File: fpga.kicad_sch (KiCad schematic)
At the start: 17 parts, among them U201 ICE40HX4K, U202 W25Q16DVSS, U203 IS61WV25616FBLL-10TLI

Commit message: Schematic update
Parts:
- added C201, C202, C203, C204, C205, C206, C207, C208, C209, C210, C211, C212, C213, C214, C215: 100n, Capacitor_SMD:C_0805_2012Metric, symbol Device:C
- C216: renamed from C201; footprint (none) -> Capacitor_SMD:CP_Elec_4x5.8; Tolerance (none) -> 20%
- C217: renamed from C202; Spec1 (none) -> 16V; Spec2 (none) -> X5R; Tolerance (none) -> 20%
- C218: renamed from C203; footprint (none) -> Capacitor_SMD:CP_Elec_4x5.8; Tolerance (none) -> 20%
- C219: renamed from C204; Spec1 (none) -> 16V; Spec2 (none) -> X5R; Tolerance (none) -> 20%
- JP201: footprint (none) -> Connector_PinHeader_2.54mm:PinHeader_2x02_P2.54mm_Vertical
- JP202: footprint (none) -> Connector_PinHeader_2.54mm:PinHeader_1x02_P2.54mm_Vertical
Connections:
- net +1.2VD: now also C201.1, C202.1, C203.1, C204.1
- net +3.3VD: now also C205.1, C206.1, C207.1, C208.1, C209.1, C210.1, C211.1, C212.1, C213.1, C214.1, C215.1
- net GND: now also C201.2, C202.2, C203.2, C204.2, C205.2, C206.2, C207.2, C208.2, C209.2, C210.2, C211.2, C212.2, C213.2, C214.2, C215.2
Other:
- moved on the sheet: C216, C217, C218, C219, JP201, JP202, R201, R202, R203, R204, R205, R206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

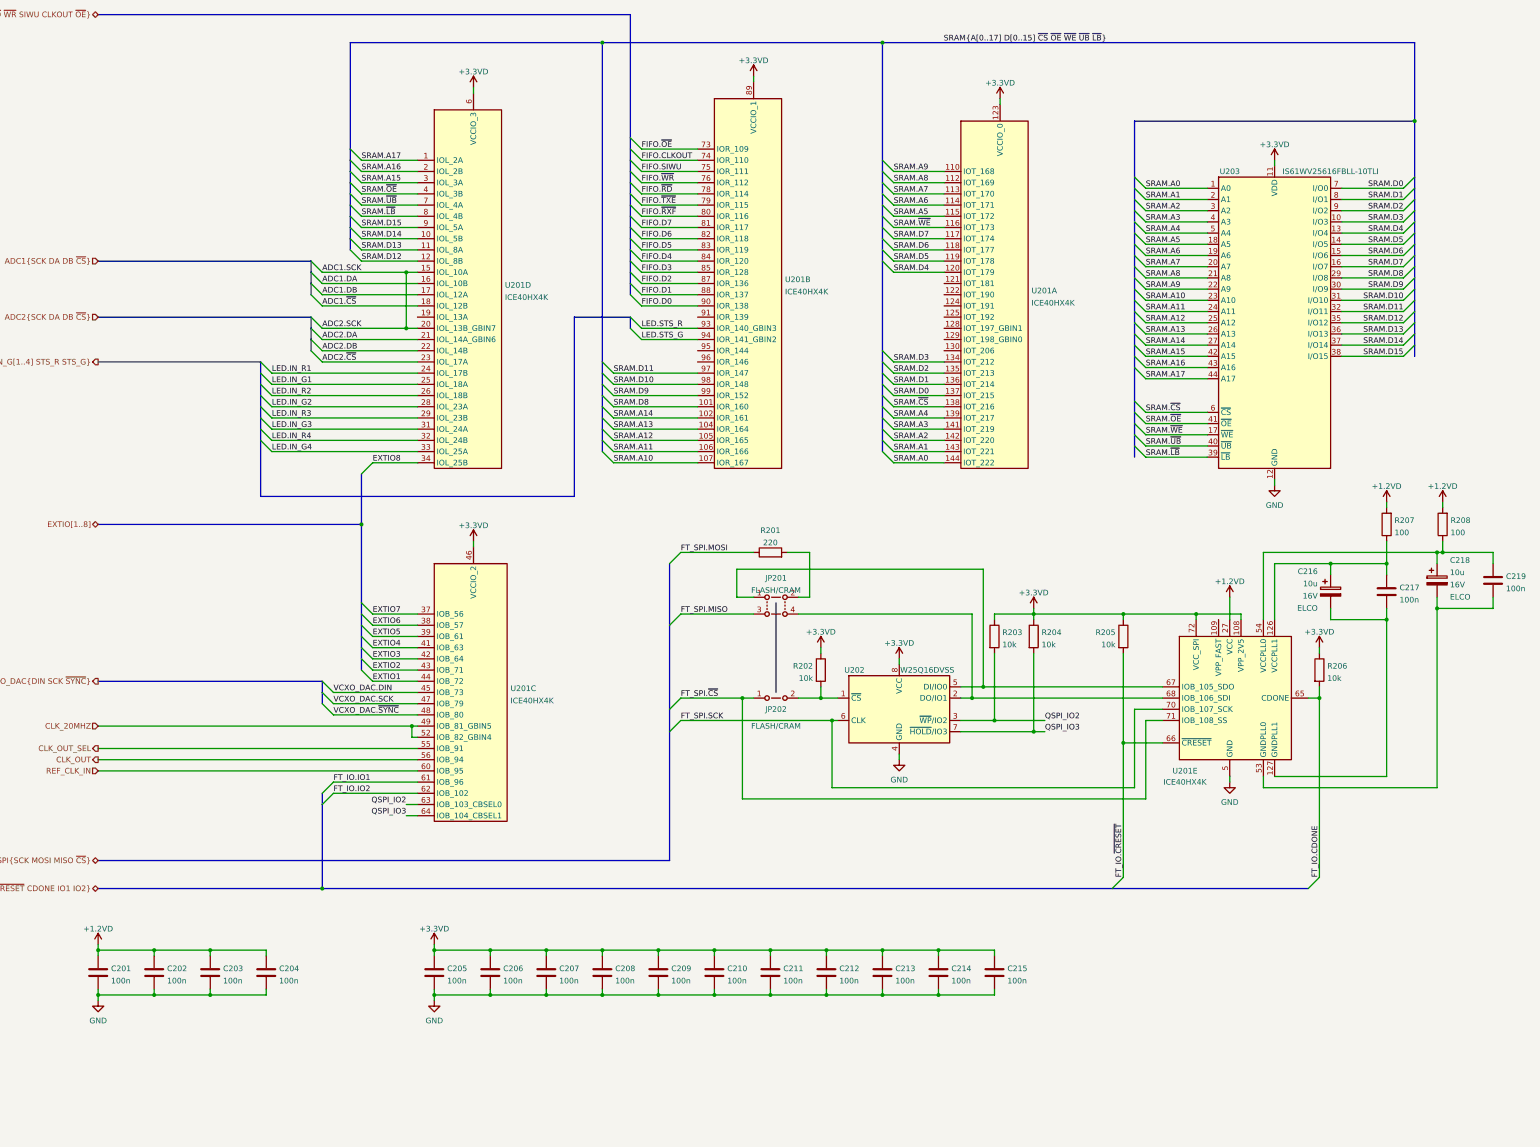
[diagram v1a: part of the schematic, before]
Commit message: Schematic: better LDO output capacitor selection, clarified BOM
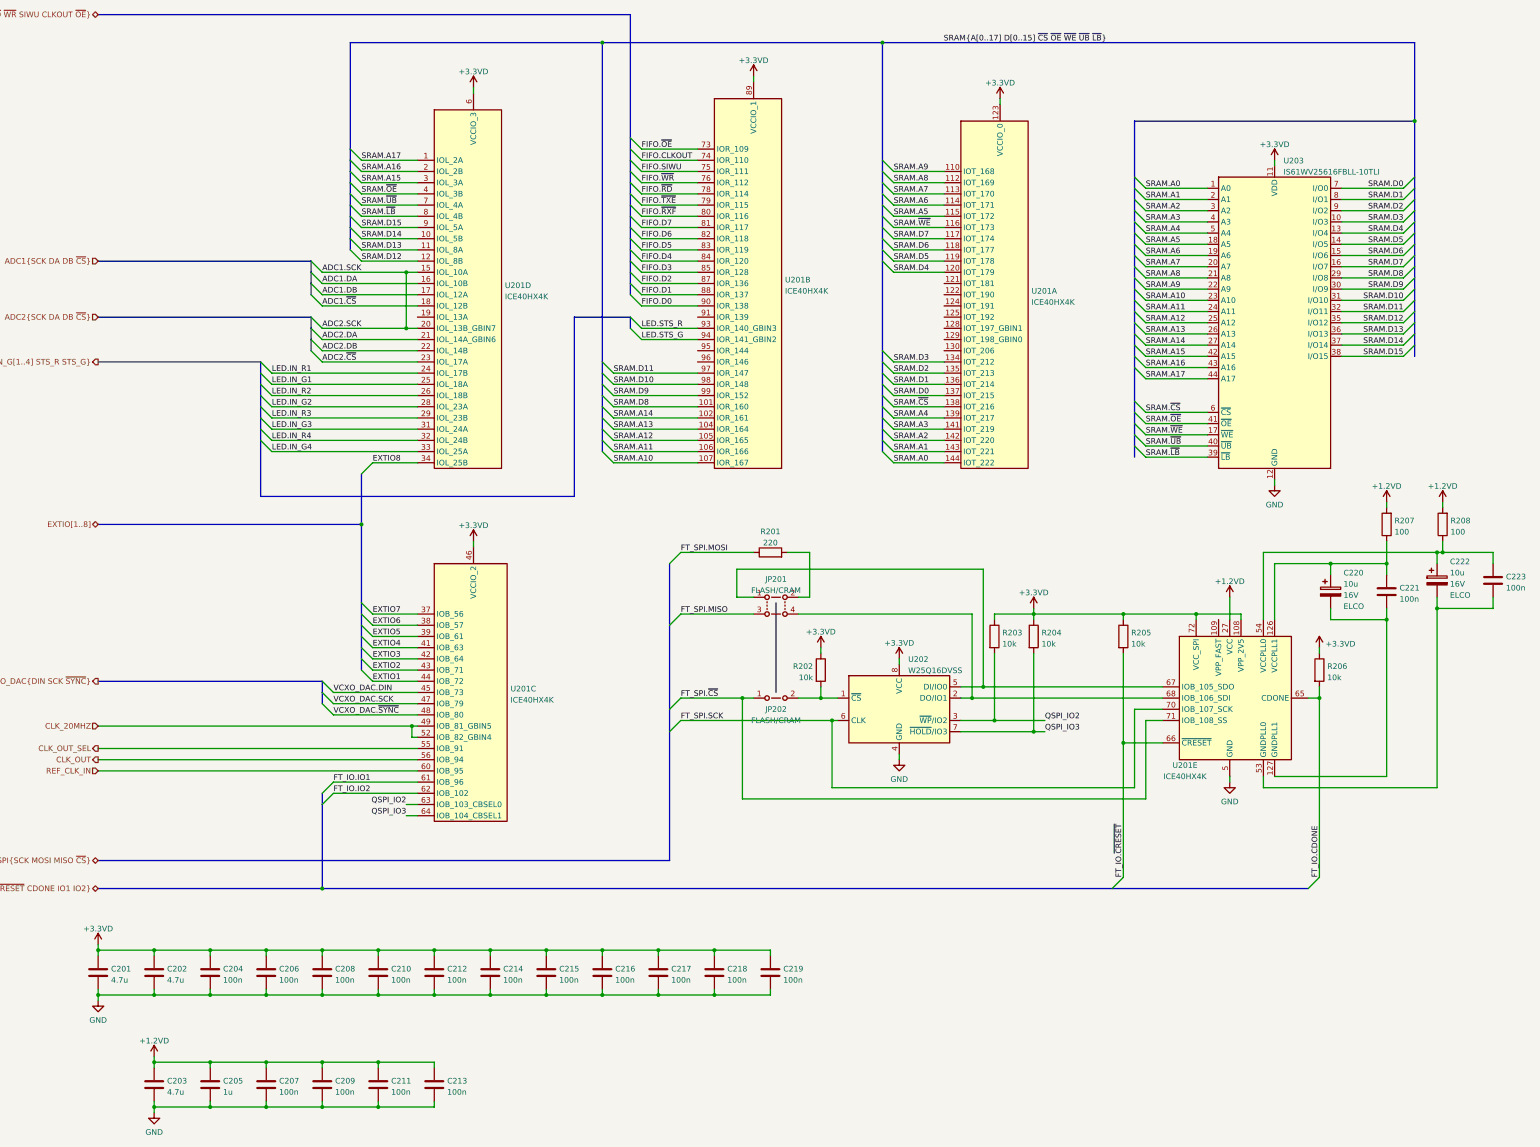
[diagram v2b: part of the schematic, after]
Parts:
- added C205: 1u, Capacitor_SMD:C_0805_2012Metric, symbol Device:C
- added C213, C218, C219: 100n, Capacitor_SMD:C_0805_2012Metric, symbol Device:C
- C201: renamed from C205; value 100n -> 4.7u; Spec1 16V -> (none); Spec2 X5R -> (none); Tolerance 20% -> (none)
- C202: renamed from C206; value 100n -> 4.7u; Spec1 16V -> (none); Spec2 X5R -> (none); Tolerance 20% -> (none)
- C203: renamed from C201; value 100n -> 4.7u; Spec1 16V -> (none); Spec2 X5R -> (none); Tolerance 20% -> (none)
- C204: renamed from C207; Spec1 16V -> (none); Spec2 X5R -> (none); Tolerance 20% -> (none)
- C206: renamed from C208; Spec1 16V -> (none); Spec2 X5R -> (none); Tolerance 20% -> (none)
- C207: renamed from C202; Spec1 16V -> (none); Spec2 X5R -> (none); Tolerance 20% -> (none)
- C208: renamed from C209; Spec1 16V -> (none); Spec2 X5R -> (none); Tolerance 20% -> (none)
- C209: renamed from C203; Spec1 16V -> (none); Spec2 X5R -> (none); Tolerance 20% -> (none)
- C210: Spec1 16V -> (none); Spec2 X5R -> (none); Tolerance 20% -> (none)
- C211: renamed from C204; Spec1 16V -> (none); Spec2 X5R -> (none); Tolerance 20% -> (none)
- C212: renamed from C211; Spec1 16V -> (none); Spec2 X5R -> (none); Tolerance 20% -> (none)
- C214: renamed from C212; Spec1 16V -> (none); Spec2 X5R -> (none); Tolerance 20% -> (none)
- C215: renamed from C213; Spec1 16V -> (none); Spec2 X5R -> (none); Tolerance 20% -> (none)
- C216: renamed from C214; Spec1 16V -> (none); Spec2 X5R -> (none); Tolerance 20% -> (none)
- C217: renamed from C215; Spec1 16V -> (none); Spec2 X5R -> (none); Tolerance 20% -> (none)
- C221: renamed from C217; Spec1 16V -> (none); Spec2 X5R -> (none); Tolerance 20% -> (none)
- C223: renamed from C219; Spec1 16V -> (none); Spec2 X5R -> (none); Tolerance 20% -> (none)
- renumbered C216 to C220, C218 to C222
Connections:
- net +1.2VD: now also C205.1, C213.1
- net +3.3VD: now also C218.1, C219.1
- net GND: now also C205.2, C213.2, C218.2, C219.2
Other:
- moved on the sheet: C201, C202, C203, C204, C206, C207, C208, C209, C210, C211, C212, C214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

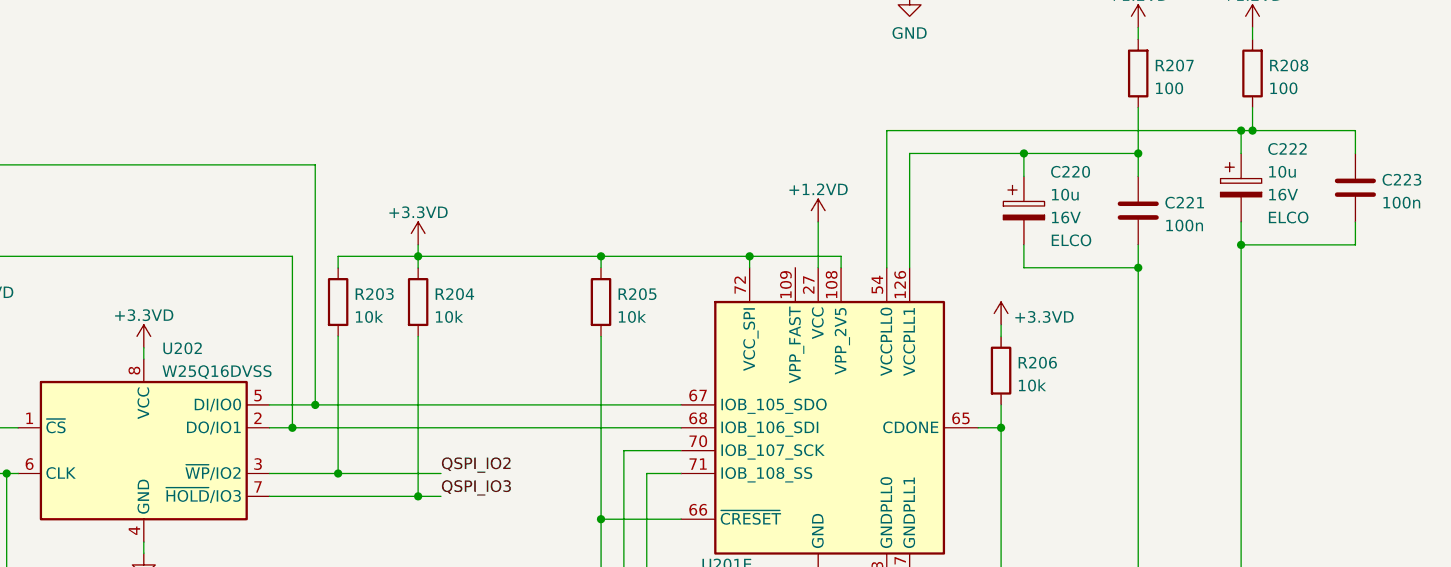
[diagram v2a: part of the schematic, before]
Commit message: Schematic: yet another update -Improve way caps are specified once again -Update cap voltages based on ESD simulation -Make anti-aliasing LC filter more practical - with much less inductors -Specify Mfr & MfrPN for almost all components (most from Mouser, some from Digikey)
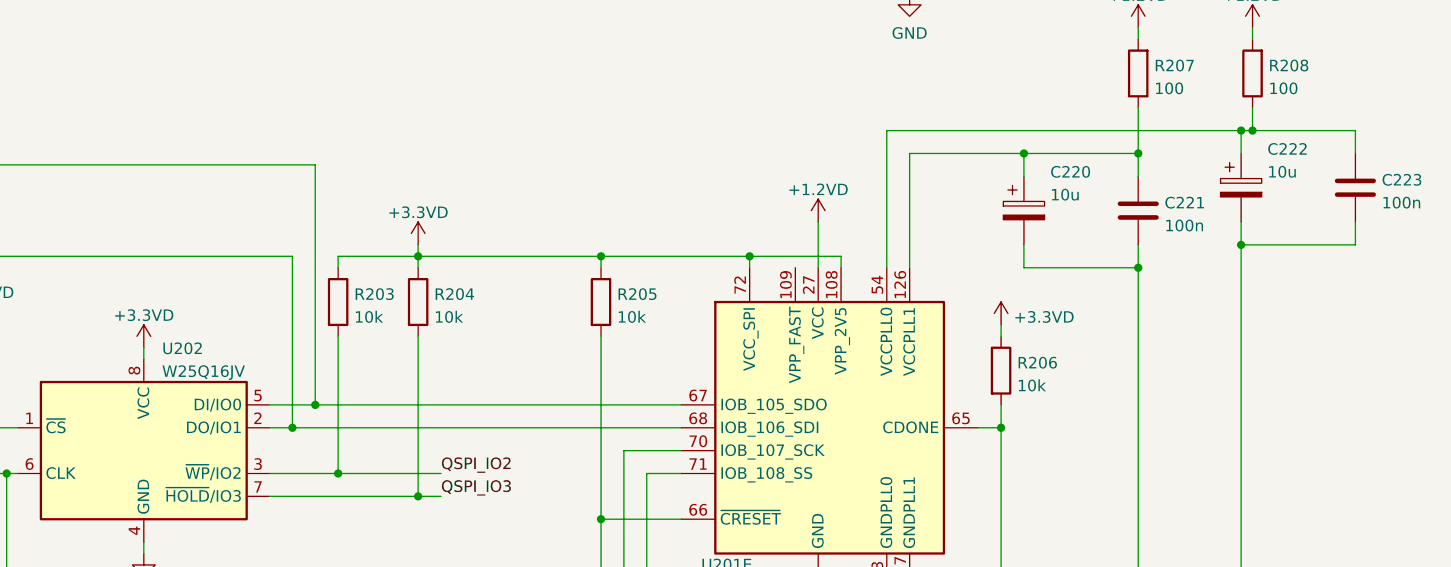
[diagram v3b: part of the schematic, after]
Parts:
- C201, C202, C203: Mfr (none) -> Murata; Mfr PN (none) -> GRM21BR71C475ME51
- C204, C206, C207, C208, C209, C210, C211, C212, C213, C214, C215, C216, C217, C218, C219, C221, C223: Mfr (none) -> Samsung; Mfr PN (none) -> CL21B104KBFNNNE
- C205: Mfr (none) -> Samsung; Mfr PN (none) -> CL21B105KOFNNNG
- C220, C222: Mfr (none) -> Nichicon; Mfr PN (none) -> UCL1C100MCL1GS; Spec1 16V -> (none); Spec2 ELCO -> (none); Tolerance 20% -> (none)
- R201, R202, R203, R204, R205, R206, R207, R208: Tolerance 5% -> (none)
- U201: Mfr (none) -> Lattice; Mfr PN (none) -> iCE40HX4K-TQ144
- U202: value W25Q16DVSS -> W25Q16JV; Mfr (none) -> Winbond; Mfr PN (none) -> W25Q16JVSSIM
- U203: Mfr (none) -> ISSI; Mfr PN (none) -> IS61WV25616FBLL-10TLI

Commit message: Schematic: add PNs for resistors
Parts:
- R201: Mfr (none) -> Bourns; Mfr PN (none) -> CR0805-FX-2200ELF
- R202, R203, R204, R205, R206: Mfr (none) -> Bourns; Mfr PN (none) -> CR0805-FX-1002ELF
- R207, R208: Mfr (none) -> Bourns; Mfr PN (none) -> CR0805-FX-1000ELF
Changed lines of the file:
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@@
+      (effects (font (size 1.27 1.27)) hide)
+    )
+    (property "Mfr" "Bourns" (id 5) (at 279.4 165.1 0)
+      (effects (font (size 1.27 1.27)) hide)
+    )
+    (property "Mfr PN" "CR0805-FX-1002ELF" (id 6) (at 279.4 165.1 0)
       (effects (font (size 1.27 1.27)) hide)
     )
@@
     )
     (property "Tolerance" "" (id 4) (at 381 139.7 0)
+      (effects (font (size 1.27 1.27)) hide)
+    )
+    (property "Mfr" "Bourns" (id 5) (at 381 139.7 0)
+      (effects (font (size 1.27 1.27)) hide)
+    )
+    (property "Mfr PN" "CR0805-FX-1000ELF" (id 6) (at 381 139.7 0)
       (effects (font (size 1.27 1.27)) hide)
     )
@@
       (effects (font (size 1.27 1.27)) hide)
     )
+    (property "Mfr" "Bourns" (id 5) (at 308.61 165.1 0)
+      (effects (font (size 1.27 1.27)) hide)
+    )
+    (property "Mfr PN" "CR0805-FX-1002ELF" (id 6) (at 308.61 165.1 0)
+      (effects (font (size 1.27 1.27)) hide)
+    )
     (pin "1")
     (pin "2")
@@
     )
     (property "Tolerance" "" (id 4) (at 368.3 139.7 0)
+      (effects (font (size 1.27 1.27)) hide)
+    )
+    (property "Mfr" "Bourns" (id 5) (at 368.3 139.7 0)
+      (effects (font (size 1.27 1.27)) hide)
+    )
+    (property "Mfr PN" "CR0805-FX-1000ELF" (id 6) (at 368.3 139.7 0)
       (effects (font (size 1.27 1.27)) hide)
     )
@@
     )
     (property "Tolerance" "" (id 4) (at 228.6 146.05 0)
+      (effects (font (size 1.27 1.27)) hide)
+    )
+    (property "Mfr" "Bourns" (id 5) (at 228.6 146.05 0)
+      (effects (font (size 1.27 1.27)) hide)
+    )
+    (property "Mfr PN" "CR0805-FX-2200ELF" (id 6) (at 228.6 146.05 0)
       (effects (font (size 1.27 1.27)) hide)
     )
@@
     )
     (property "Tolerance" "" (id 4) (at 288.29 165.1 0)
+      (effects (font (size 1.27 1.27)) hide)
+    )
+    (property "Mfr" "Bourns" (id 5) (at 288.29 165.1 0)
+      (effects (font (size 1.27 1.27)) hide)
+    )
+    (property "Mfr PN" "CR0805-FX-1002ELF" (id 6) (at 288.29 165.1 0)
       (effects (font (size 1.27 1.27)) hide)
     )
@@
       (effects (font (size 1.27 1.27)) hide)
     )
+    (property "Mfr" "Bourns" (id 5) (at 353.06 172.72 0)
+      (effects (font (size 1.27 1.27)) hide)
+    )
+    (property "Mfr PN" "CR0805-FX-1002ELF" (id 6) (at 353.06 172.72 0)
+      (effects (font (size 1.27 1.27)) hide)
+    )
     (pin "1")
     (pin "2")
@@
       (effects (font (size 1.27 1.27)) hide)
     )
+    (property "Mfr" "Bourns" (id 5) (at 240.03 172.72 0)
+      (effects (font (size 1.27 1.27)) hide)
+    )
+    (property "Mfr PN" "CR0805-FX-1002ELF" (id 6) (at 240.03 172.72 0)
+      (effects (font (size 1.27 1.27)) hide)
+    )
